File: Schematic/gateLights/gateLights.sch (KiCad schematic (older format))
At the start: 2 parts, among them J1 CONN_01X06, J3 CONN_01X02

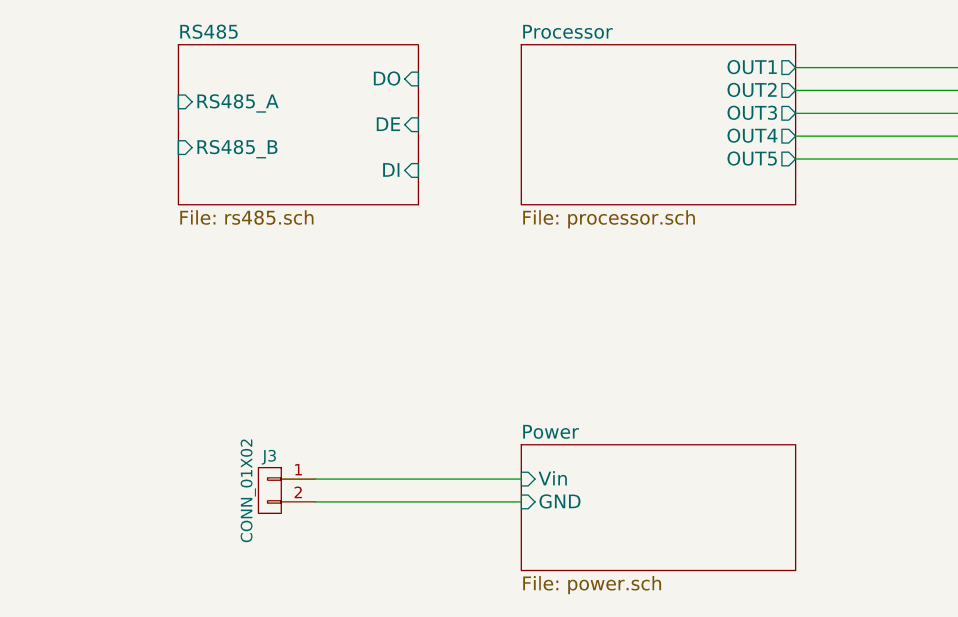
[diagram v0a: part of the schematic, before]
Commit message: RS485 protection
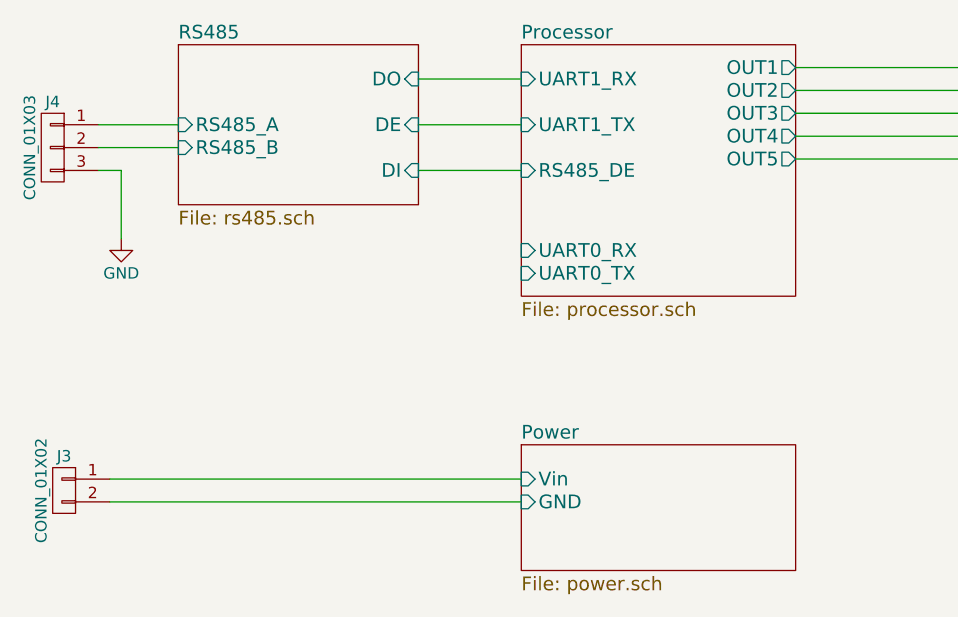
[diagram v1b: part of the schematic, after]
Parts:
- added J4: CONN_01X03, Pin_Headers:Pin_Header_Straight_1x03_Pitch2.54mm, symbol CONN_01X03
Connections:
- net RS485/RS485_A: now also J4.1 (P1)
- net RS485/RS485_B: now also J4.2 (P2)
- new net GND: J4.3 (P3)
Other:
- moved on the sheet: J3
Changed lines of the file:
@@
 $EndDescr
 $Sheet
-S 3050 2700 1200 700
+S 3050 2700 1200 1100
 U 592040A2
 F0 "Processor" 60
@@
 F5 "OUT4" O R 4250 3100 60
 F6 "OUT5" O R 4250 3200 60
+F7 "UART1_TX" I L 3050 3050 60
+F8 "UART1_RX" I L 3050 2850 60
+F9 "UART0_RX" I L 3050 3600 60
+F10 "UART0_TX" I L 3050 3700 60
+F11 "RS485_DE" I L 3050 3250 60
 $EndSheet
 $Sheet
@@
 L CONN_01X02 J3
 U 1 1 592076EA
-P 1950 4650
-F 0 "J3" H 1950 4800 50  0000 C CNN
-F 1 "CONN_01X02" V 2050 4650 50  0000 C CNN
-F 2 "Pin_Headers:Pin_Header_Straight_1x02_Pitch2.54mm" H 1950 4650 50  0001 C CNN
-F 3 "" H 1950 4650 50  0001 C CNN
-	1    1950 4650
+P 1050 4650
+F 0 "J3" H 1050 4800 50  0000 C CNN
+F 1 "CONN_01X02" V 1150 4650 50  0000 C CNN
+F 2 "Pin_Headers:Pin_Header_Straight_1x02_Pitch2.54mm" H 1050 4650 50  0001 C CNN
+F 3 "" H 1050 4650 50  0001 C CNN
+	1    1050 4650
 	-1   0    0    -1
 $EndComp
@@
 	5100 3200 4250 3200
 Wire Wire Line
-	2150 4600 3050 4600
+	1250 4600 3050 4600
 Wire Wire Line
-	3050 4700 2150 4700
+	3050 4700 1250 4700
 $Sheet
 S 1550 2700 1050 700
@@
 F0 "RS485" 60
 F1 "rs485.sch" 60
-F2 "RS485_A" I L 1550 2950 60
+F2 "RS485_A" I L 1550 3050 60
 F3 "RS485_B" I L 1550 3150 60
 F4 "DE" I R 2600 3050 60
@@
 F6 "DI" I R 2600 3250 60
 $EndSheet
+$Comp
+L CONN_01X03 J4
+U 1 1 5923CDB5
+P 1000 3150
+F 0 "J4" H 1000 3350 50  0000 C CNN
+F 1 "CONN_01X03" V 1100 3150 50  0000 C CNN
+F 2 "Pin_Headers:Pin_Header_Straight_1x03_Pitch2.54mm" H 1000 3150 50  0001 C CNN
+F 3 "" H 1000 3150 50  0001 C CNN
+	1    1000 3150
+	-1   0    0    -1
+$EndComp
+$Comp
+L GND #PWR1
+U 1 1 5923CF80
+P 1300 3550
+F 0 "#PWR1" H 1300 3300 50  0001 C CNN
+F 1 "GND" H 1300 3400 50  0000 C CNN
+F 2 "" H 1300 3550 50  0001 C CNN
+F 3 "" H 1300 3550 50  0001 C CNN
+	1    1300 3550
+	1    0    0    -1
+$EndComp
+Wire Wire Line
+	1200 3250 1300 3250
+Wire Wire Line
+	1300 3250 1300 3550
+Wire Wire Line
+	1550 3050 1200 3050
+Wire Wire Line
+	1200 3150 1550 3150
+Wire Wire Line
+	3050 2850 2600 2850
+Wire Wire Line
+	2600 3050 3050 3050
+Wire Wire Line
+	3050 3250 2600 3250
 $EndSCHEMATC

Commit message: Add inputs
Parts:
- added J5: CONN_01X04, Pin_Headers:Pin_Header_Straight_1x04_Pitch2.54mm, symbol CONN_01X04
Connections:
- net GND: now also J5.4 (P4)
- new net Input/IN_1: J5.1 (P1)
- new net Input/IN_2: J5.2 (P2)
- new net Input/IN_3: J5.3 (P3)
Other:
- moved on the sheet: J3
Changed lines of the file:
@@
 $Descr A4 11693 8268
 encoding utf-8
-Sheet 1 5
+Sheet 1 6
 Title "Running Gate Lights"
 Date "2017-05-20"
@@
 $EndDescr
 $Sheet
-S 3050 2700 1200 1100
+S 3050 2700 1200 2550
 U 592040A2
 F0 "Processor" 60
@@
 F10 "UART0_TX" I L 3050 3700 60
 F11 "RS485_DE" I L 3050 3250 60
+F12 "IN_1" I L 3050 4700 60
+F13 "IN_2" I L 3050 4800 60
+F14 "IN_3" I L 3050 4900 60
 $EndSheet
 $Sheet
@@
 $EndComp
 $Sheet
-S 3050 4450 1200 550
+S 3050 5550 1200 550
 U 5920687E
 F0 "Power" 60
 F1 "power.sch" 60
-F2 "Vin" I L 3050 4600 60
-F3 "GND" I L 3050 4700 60
+F2 "Vin" I L 3050 5700 60
+F3 "GND" I L 3050 5800 60
 $EndSheet
 $Comp
 L CONN_01X02 J3
 U 1 1 592076EA
-P 1050 4650
-F 0 "J3" H 1050 4800 50  0000 C CNN
-F 1 "CONN_01X02" V 1150 4650 50  0000 C CNN
-F 2 "Pin_Headers:Pin_Header_Straight_1x02_Pitch2.54mm" H 1050 4650 50  0001 C CNN
-F 3 "" H 1050 4650 50  0001 C CNN
-	1    1050 4650
+P 1050 5750
+F 0 "J3" H 1050 5900 50  0000 C CNN
+F 1 "CONN_01X02" V 1150 5750 50  0000 C CNN
+F 2 "Pin_Headers:Pin_Header_Straight_1x02_Pitch2.54mm" H 1050 5750 50  0001 C CNN
+F 3 "" H 1050 5750 50  0001 C CNN
+	1    1050 5750
 	-1   0    0    -1
 $EndComp
@@
 	5100 3200 4250 3200
 Wire Wire Line
-	1250 4600 3050 4600
-Wire Wire Line
-	3050 4700 1250 4700
+	1250 5700 3050 5700
+Wire Wire Line
+	3050 5800 1250 5800
 $Sheet
 S 1550 2700 1050 700
@@
 $EndComp
 $Comp
-L GND #PWR1
+L GND #PWR01
 U 1 1 5923CF80
 P 1300 3550
-F 0 "#PWR1" H 1300 3300 50  0001 C CNN
+F 0 "#PWR01" H 1300 3300 50  0001 C CNN
 F 1 "GND" H 1300 3400 50  0000 C CNN
 F 2 "" H 1300 3550 50  0001 C CNN
@@
 Wire Wire Line
 	3050 3250 2600 3250
+$Sheet
+S 1650 4550 1000 500
+U 5926FBF0
+F0 "Input" 60
+F1 "input.sch" 60
+F2 "IN_1" I L 1650 4700 60
+F3 "OUT_1" O R 2650 4700 60
+F4 "IN_2" I L 1650 4800 60
+F5 "OUT_2" O R 2650 4800 60
+F6 "IN_3" I L 1650 4900 60
+F7 "OUT_3" O R 2650 4900 60
+$EndSheet
+$Comp
+L CONN_01X04 J5
+U 1 1 5927301C
+P 1050 4850
+F 0 "J5" H 1050 5100 50  0000 C CNN
+F 1 "CONN_01X04" V 1150 4850 50  0000 C CNN
+F 2 "Pin_Headers:Pin_Header_Straight_1x04_Pitch2.54mm" H 1050 4850 50  0001 C CNN
+F 3 "" H 1050 4850 50  0001 C CNN
+	1    1050 4850
+	-1   0    0    -1
+$EndComp
+Wire Wire Line
+	1250 4700 1650 4700
+Wire Wire Line
+	1250 4800 1650 4800
+Wire Wire Line
+	1250 4900 1650 4900
+$Comp
+L GND #PWR02
+U 1 1 59273BAE
+P 1300 5100
+F 0 "#PWR02" H 1300 4850 50  0001 C CNN
+F 1 "GND" H 1300 4950 50  0000 C CNN
+F 2 "" H 1300 5100 50  0001 C CNN
+F 3 "" H 1300 5100 50  0001 C CNN
+	1    1300 5100
+	1    0    0    -1
+$EndComp
+Wire Wire Line
+	1250 5000 1300 5000
+Wire Wire Line
+	1300 5000 1300 5100
+Wire Wire Line
+	2650 4700 3050 4700
+Wire Wire Line
+	2650 4800 3050 4800
+Wire Wire Line
+	2650 4900 3050 4900
 $EndSCHEMATC

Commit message: Fix resistor footprints
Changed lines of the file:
@@
 F2 "RS485_A" I L 1550 3050 60
 F3 "RS485_B" I L 1550 3150 60
-F4 "DE" I R 2600 3050 60
+F4 "DE" I R 2600 3250 60
 F5 "DO" I R 2600 2850 60
-F6 "DI" I R 2600 3250 60
+F6 "DI" I R 2600 3050 60
 $EndSheet
 $Comp
@@
 Wire Wire Line
 	3050 2850 2600 2850
-Wire Wire Line
-	2600 3050 3050 3050
-Wire Wire Line
-	3050 3250 2600 3250
 $Sheet
 S 1650 4550 1000 500
@@
 Wire Wire Line
 	2650 4900 3050 4900
+Wire Wire Line
+	2600 3050 3050 3050
+Wire Wire Line
+	2600 3250 3050 3250
 $EndSCHEMATC
